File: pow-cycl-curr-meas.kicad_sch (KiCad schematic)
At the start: 56 parts

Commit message: Fixed FTDI sheet
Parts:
- C21, C23, C28, C29, C30, C31, C32: value (none) -> C_100n_0402; footprint (none) -> nuc-compute-cluster-power-breakout-footprints:0402-cap
- C22: value (none) -> C_1u_0402; footprint (none) -> nuc-compute-cluster-power-breakout-footprints:0402-cap
- Q1, Q2, Q5, Q7, Q8: value (none) -> SQS401EN-T1_BE3; footprint (none) -> nuc-compute-cluster-power-breakout-footprints:Vishay_PowerPAK_1212-8_Single
- Q10, Q3, Q4, Q6, Q9: value (none) -> SSM3K15ACT; footprint (none) -> nuc-compute-cluster-power-breakout-footprints:SSM3K15ACT
- R13, R14, R15, R16, R17, R18, R30, R31, R32, R33: value (none) -> R_0R_0402; footprint (none) -> nuc-compute-cluster-power-breakout-footprints:0402-res
- R19, R22, R23, R25, R28, R29: value (none) -> R_4k7_0402; footprint (none) -> nuc-compute-cluster-power-breakout-footprints:0402-res
- R20, R21, R24, R26, R27: value (none) -> R_10k_0402; footprint (none) -> nuc-compute-cluster-power-breakout-footprints:0402-res
- TP_ADC1, TP_ADC2, TP_ADC3, TP_ADC4, TP_ADC5, TP_PC1, TP_PC2, TP_PC3, TP_PC4, TP_PC5: value (none) -> TP_SMD1MM; footprint (none) -> nuc-compute-cluster-power-breakout-footprints:Testpoint_smd_1mm
- U10: value (none) -> TCA9534; footprint (none) -> nuc-compute-cluster-power-breakout-footprints:TSSOP-16
- U11, U12, U13, U8, U9: value (none) -> TMCS1100A2-Q1; footprint (none) -> nuc-compute-cluster-power-breakout-footprints:SOIC-8_W3.9mm
- U14: value (none) -> ADS7828; footprint (none) -> nuc-compute-cluster-power-breakout-footprints:TSSOP-16_4.4x5mm_P0.65mm

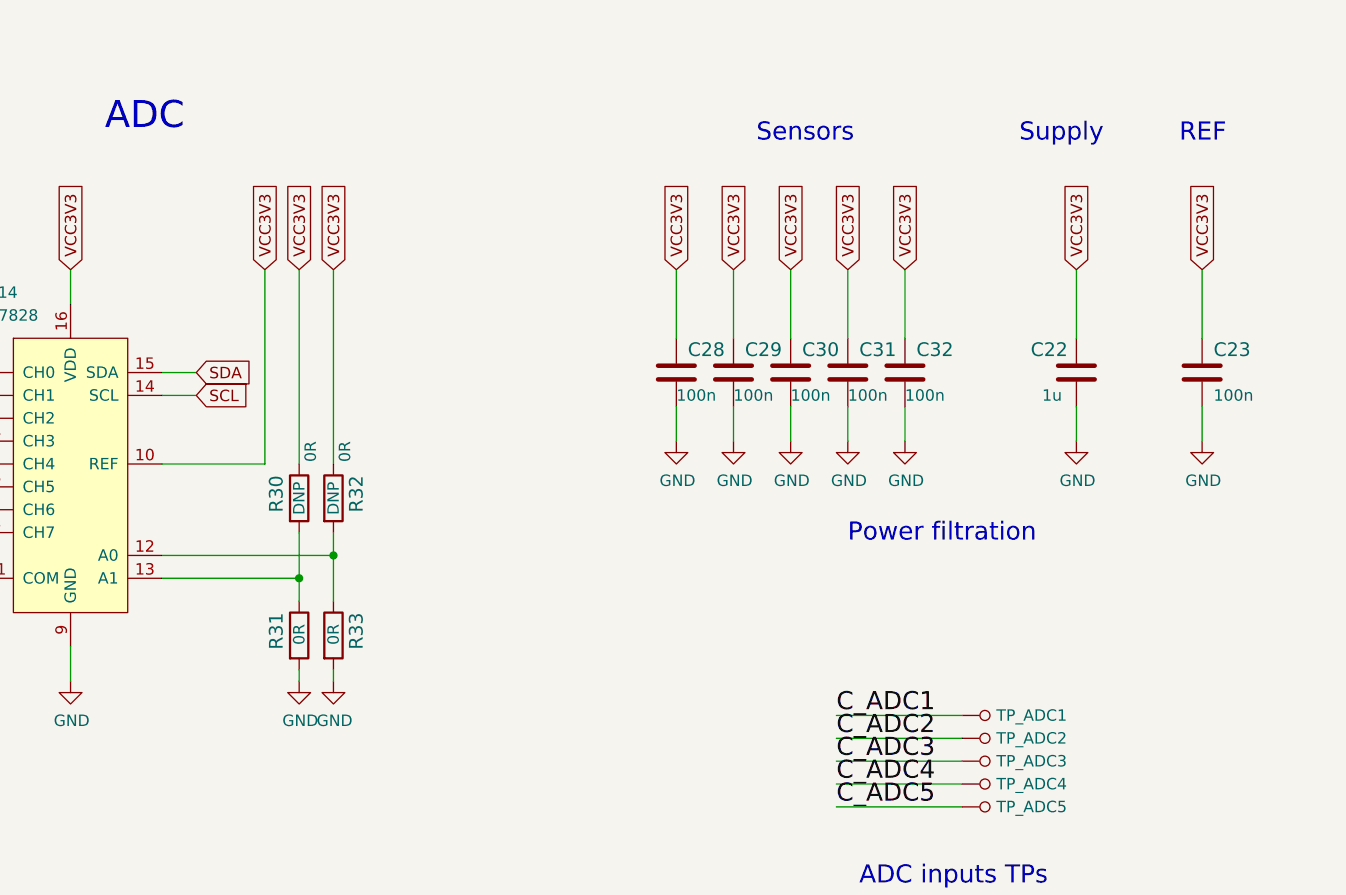
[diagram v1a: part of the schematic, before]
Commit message: Layout of power connectors
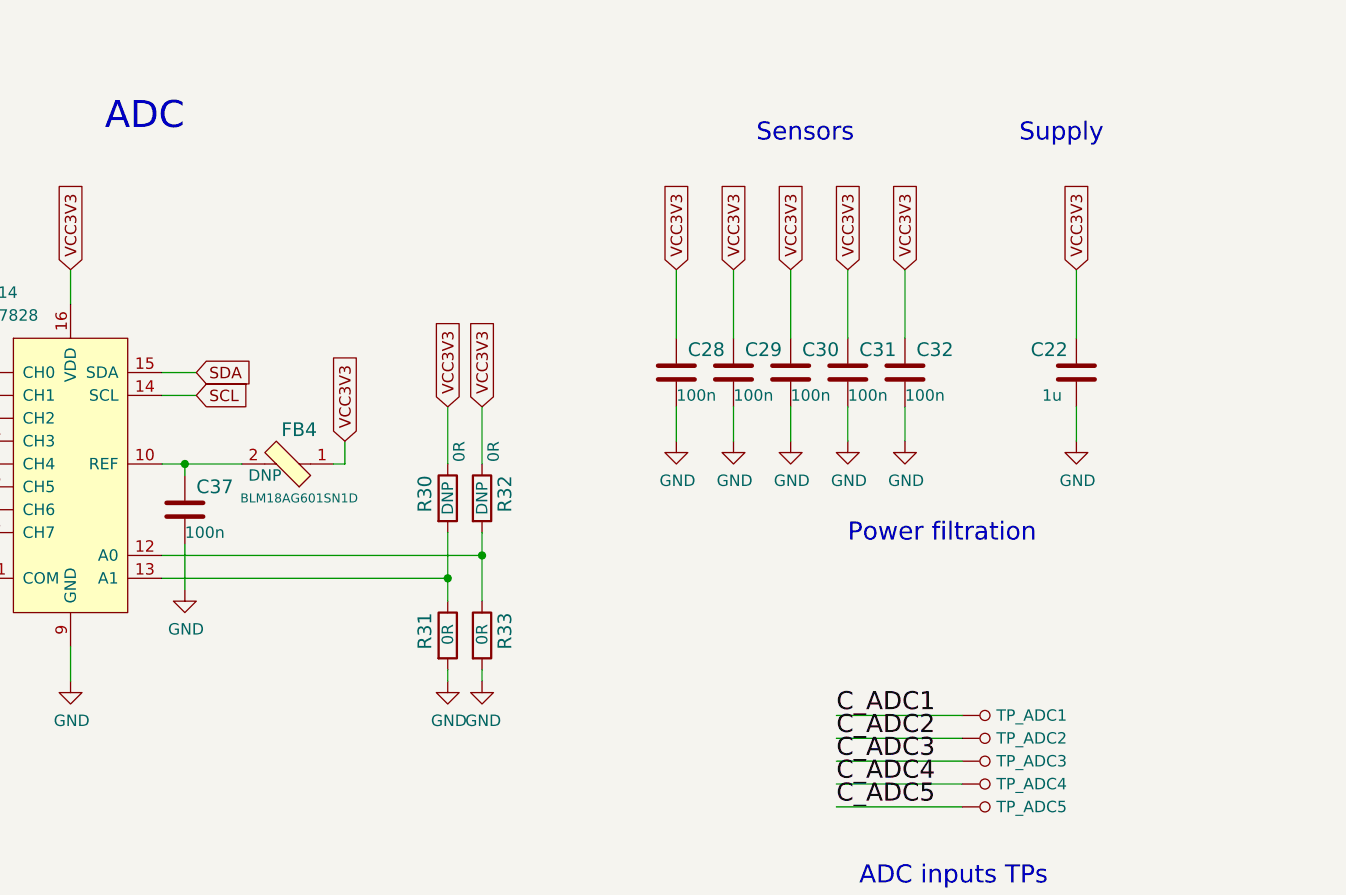
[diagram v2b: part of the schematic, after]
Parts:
- removed C23: C_100n_0402, nuc-compute-cluster-power-breakout-footprints:0402-cap, symbol nuc-compute-cluster-power-breakout:C_100n_0402
- added C37: C_100n_0402, nuc-compute-cluster-power-breakout-footprints:0402-cap, symbol nuc-compute-cluster-power-breakout:C_100n_0402
- added FB4: BLM18AG601SN1D, nuc-compute-cluster-power-breakout-footprints:0603, symbol nuc-compute-cluster-power-breakout:BLM18AG601SN1D
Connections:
- net GND: now also C37.2
- net VCC3V3: now also FB4.1; no longer U14.10 (REF)
- new net: C37.1, FB4.2, U14.10 (REF)
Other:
- note removed: "REF"
- moved on the sheet: R30, R31, R32, R33

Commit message: Revision bump to 1.3.0
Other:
- title: Power Cycling & Current Measurement Module -> NUC Computer Cluster Power Breakout HW
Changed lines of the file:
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@@
   (paper "A3")
   (title_block
-    (title "Power Cycling & Current Measurement Module")
-    (date "2022-03-07")
-    (rev "1.1")
+    (title "NUC Computer Cluster Power Breakout HW")
+    (date "2022-07-29")
+    (rev "1.3.0")
     (company "Antmicro LTD")
   )

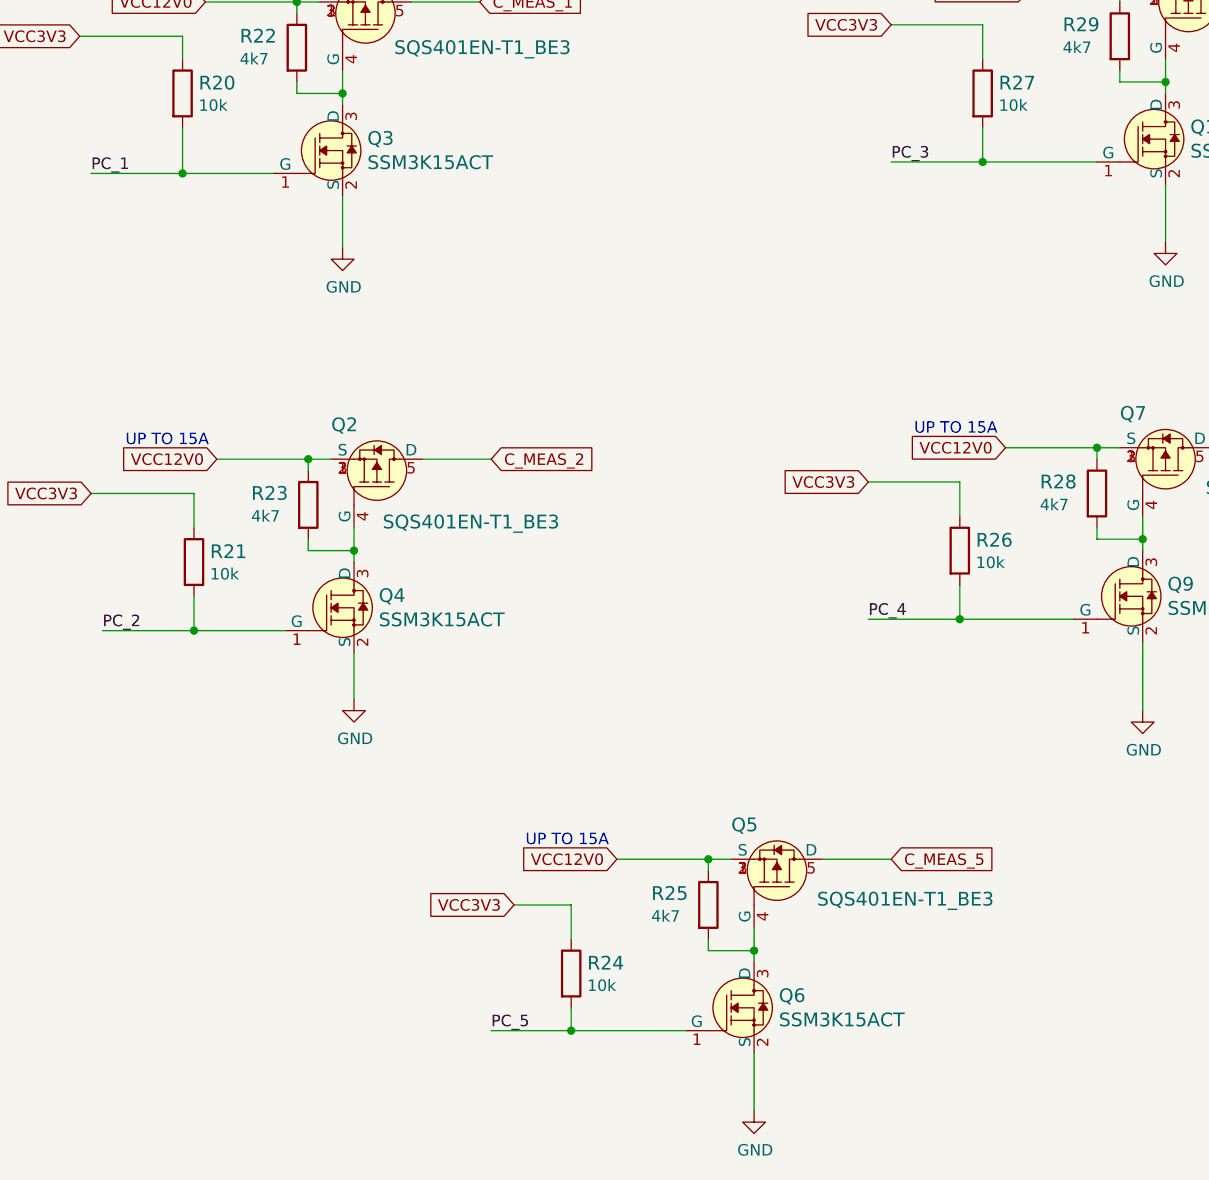
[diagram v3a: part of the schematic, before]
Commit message: Added support for default off and changed converter cap voltage rating
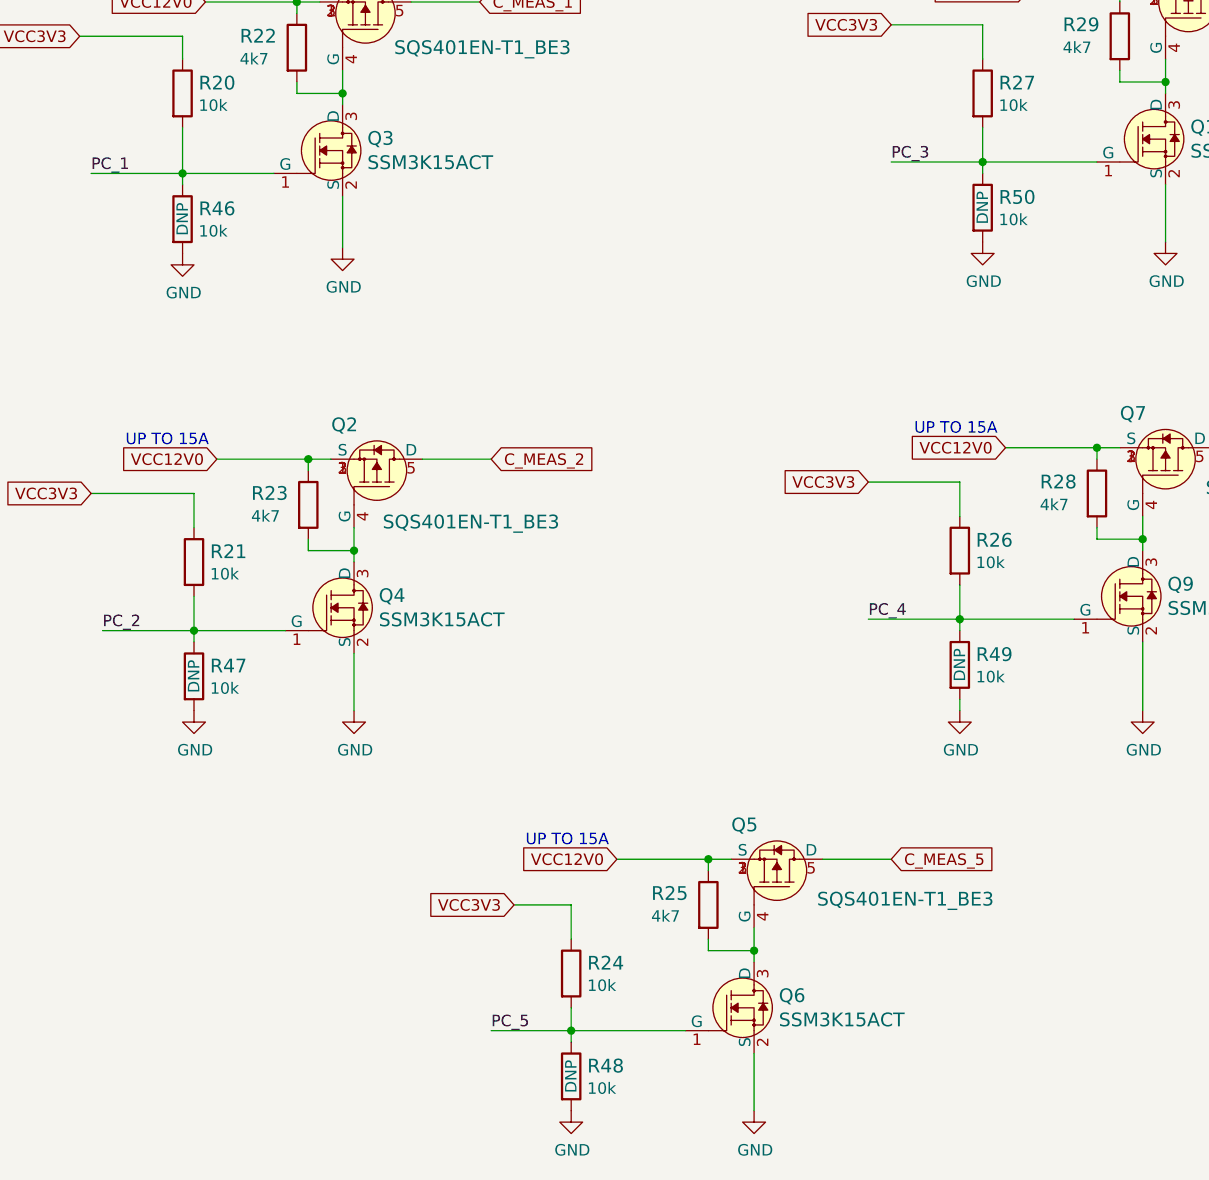
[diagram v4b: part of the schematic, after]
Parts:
- added R46, R47, R48, R49, R50: R_10k_0402, nuc-compute-cluster-power-breakout-footprints:0402-res, symbol nuc-compute-cluster-power-breakout:R_10k_0402
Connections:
- net GND: now also R46.2, R47.2, R48.2, R49.2, R50.2
- net PC_1: now also R46.1
- net PC_2: now also R47.1
- net PC_3: now also R50.1
- net PC_4: now also R49.1
- net PC_5: now also R48.1
